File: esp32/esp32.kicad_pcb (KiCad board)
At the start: 2 copper layers, 35 x 17 mm, 23 parts, among them J1 Conn_01x06_Pin, J2 Conn_01x06_Pin, J4 Conn_01x06_Pin, J5 USB_C_Receptacle_USB2.0_14P, Q1 MMSS8050, Q2 MMSS8050, SW1 XUNPU TS-1088R-02526, U1 SPX3819M5-L-3-3, U2 CP2102N-Axx-xQFN28

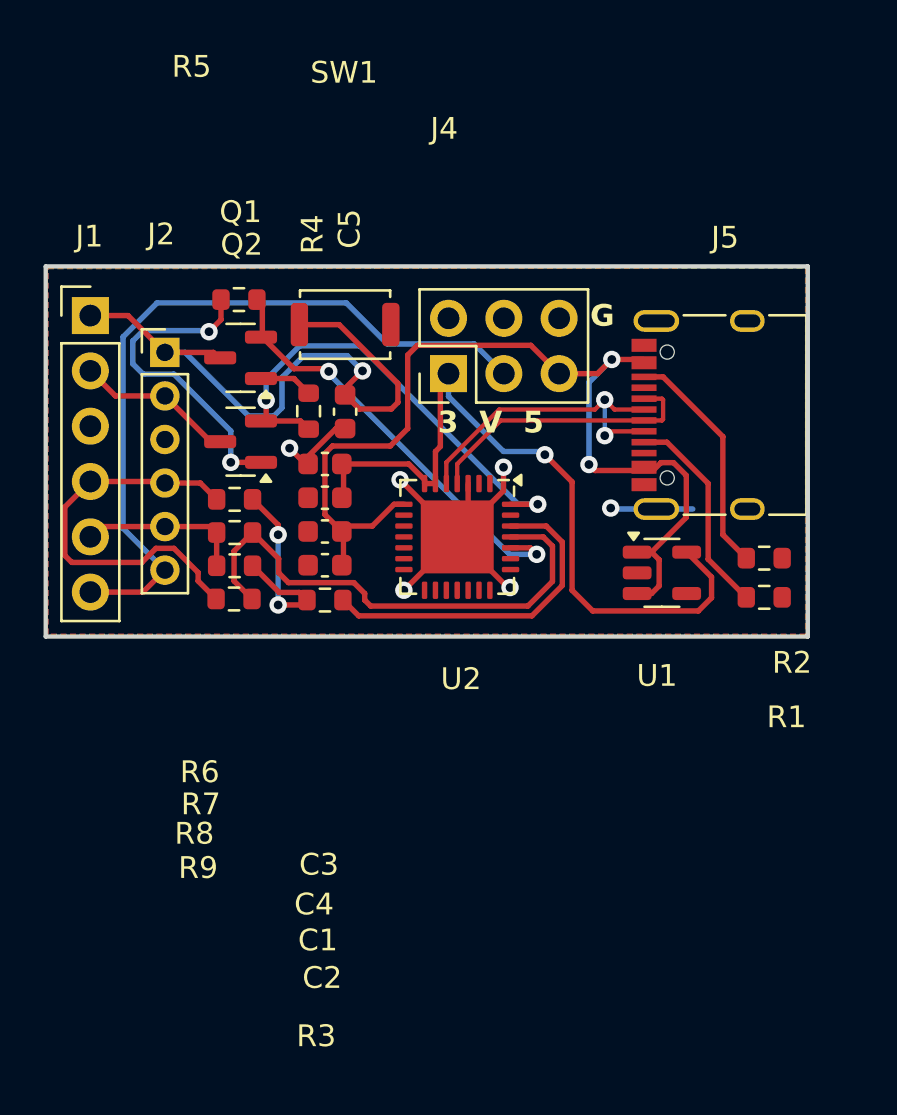
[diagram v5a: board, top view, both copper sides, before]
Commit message: esp32: remove R on TX
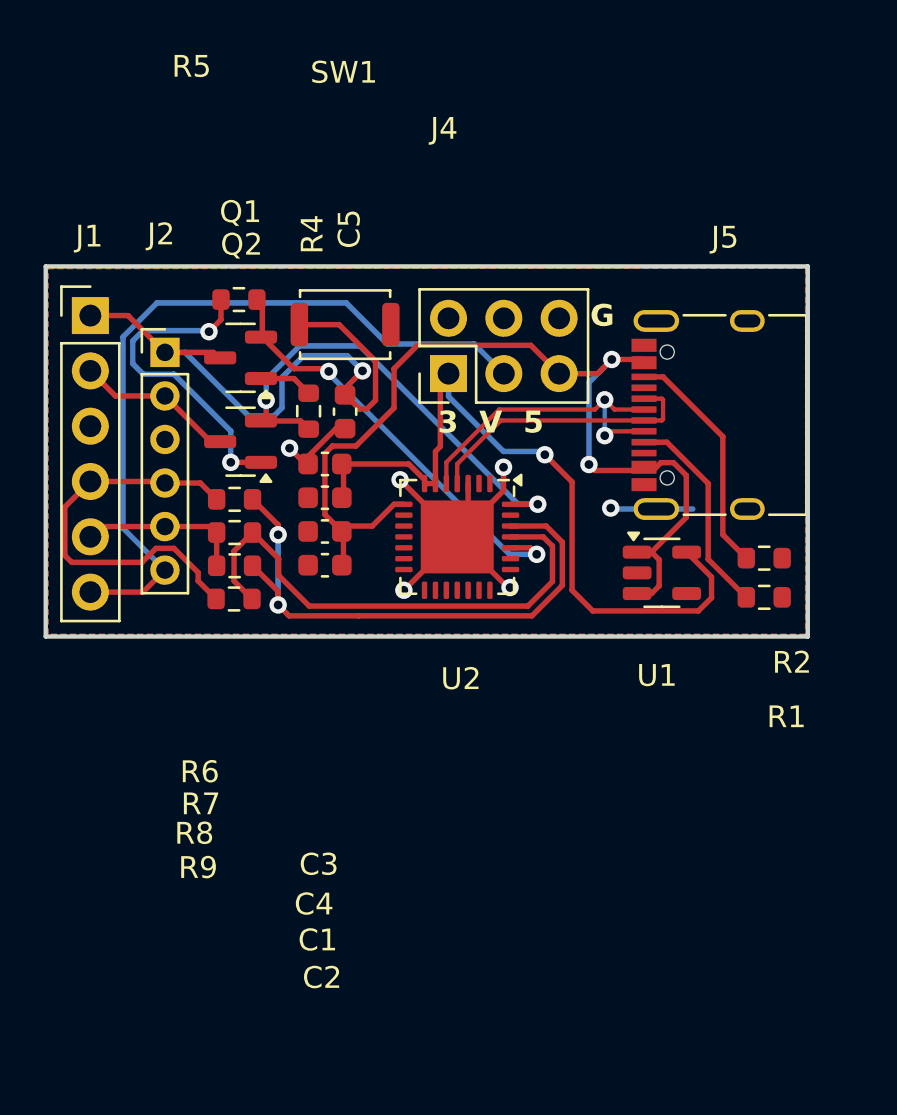
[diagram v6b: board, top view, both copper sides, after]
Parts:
- removed R3: 470, Resistor_SMD:R_0603_1608Metric
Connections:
- U2 pad 26: Net-(U2-TXD) -> /TXD
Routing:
- net /TXD: track 9.91 -> 26.1 mm
- net Net-(U2-TXD): track 15.6 -> 0.00 mm
- net /EN: track 30.0 -> 28.5 mm
- net /5V: track 46.4 -> 45.4 mm
